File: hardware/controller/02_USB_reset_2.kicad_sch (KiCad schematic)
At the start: 7 parts, among them SW1 RESET, SW2 BOOT, SW3 START, SW4 STOP / hold reset

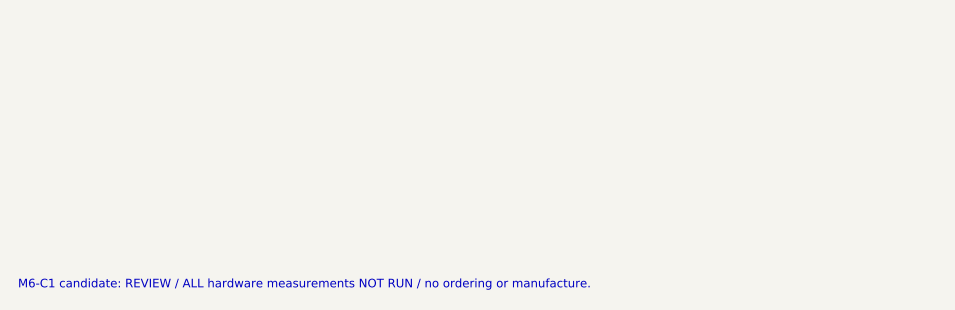
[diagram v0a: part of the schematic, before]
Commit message: M6-C1R1: protect pack identity input and review USB ESD topology
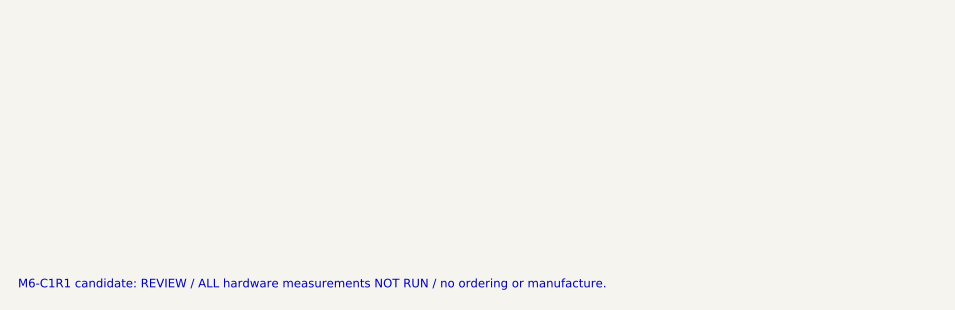
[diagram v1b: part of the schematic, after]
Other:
- note added: "M6-C1R1 candidate: REVIEW / ALL hardware measurements NOT RUN / no ordering or manufacture."
- note removed: "M6-C1 candidate: REVIEW / ALL hardware measurements NOT RUN / no ordering or manufacture."
